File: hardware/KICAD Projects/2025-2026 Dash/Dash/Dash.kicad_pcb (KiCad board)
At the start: 2 copper layers, 200 x 75 mm, 41 parts, among them J1 TACH-SERVO, J2 SPEED-SERVO, J3 5V INPUT, J4 UPPER Button, J5 TO CAN CONNECTOR, J6 LOWER Button, U1 XIAO-ESP32-S3-SMD, U3 EA DOGM128W-6, Y1 ABM10AIG-16.000MHZ-4Z-T3

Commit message: Dash R1 Milestone
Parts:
- removed J3: 5V INPUT, Connector_Wire:SolderWire-0.75sqmm_1x02_P4.8mm_D1.25mm_OD2.3mm
- removed J5: TO CAN CONNECTOR, Connector_Wire:SolderWire-0.75sqmm_1x04_P4.8mm_D1.25mm_OD2.3mm
- removed the LOWER_AlphaDriver at (228.0, 108.4)
- removed the UPPER_AlphaDriver at (228.0, 83.9)
- added J7: DTF13-6P, DTF13-6P:TE_DTF13-6P, B.Cu at (232.8, 115.5)
- added LOWER_AlphaDriver: Alphanumeric Driver LOWER, Adafruit HT16K33 Breakout (Laptop):DIP1778W100P254L3556H630Q28N, B.Cu at (185.6, 105.6)
- added UPPER_AlphaDriver: Alphanumeric Driver UPPER, Adafruit HT16K33 Breakout (Laptop):DIP1778W100P254L3556H630Q28N, B.Cu at (185.8, 75.5)
- IC1: renamed from CAN CAN
- LOWER_D1-2, LOWER_D3-4, UPPER_D1-2, UPPER_D3-4: footprint Adafruit Dual Alphanumeric LED:1908 -> Adafruit Dual Alphanumeric LED (Laptop):1908
- moved G*** 164.8 mm to (230.6, 83.5)
- moved R1 53.9 mm to (138.6, 67.0)
- moved R2 49.4 mm to (138.6, 69.0)
- moved U3 48.0 mm to (152.0, 73.5), turned to -90 degrees
- moved C1 47.1 mm to (103.8, 120.4), turned to 90 degrees
- moved R3 44.9 mm to (138.6, 71.0)
- moved C2 44.6 mm to (106.2, 120.4), turned to 90 degrees
- moved C3 42.4 mm to (108.8, 120.4), turned to 90 degrees
- moved C4 40.4 mm to (111.4, 120.4), turned to 90 degrees
- moved J4 38.5 mm to (86.7, 60.0)
- moved C5 36.6 mm to (114.8, 119.5), turned to 180 degrees
- moved C6 33.9 mm to (120.0, 119.5), turned to 0 degrees
- moved C7 32.3 mm to (124.8, 119.5), turned to 0 degrees
- moved C8 32.2 mm to (129.2, 120.4), turned to 90 degrees
- moved C9 31.6 mm to (132.8, 119.5), turned to 0 degrees
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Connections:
- IC1 pad 26: GND -> CAN_GND
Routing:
- net GND: track 684.4 -> 568.1 mm, vias 7 -> 5
- net ROW14_UPPER: track 156.0 -> 44.5 mm, vias 3 -> 0
- net CAN_HIGH: track 69.2 -> 161.7 mm, vias 0 -> 2
- net ROW0_UPPER: track 141.0 -> 52.7 mm, vias 0 -> 1
- net CAN_LOW: track 63.9 -> 150.7 mm, vias 0 -> 2
- net COM_Digit1_LOWER: track 121.3 -> 38.4 mm
- net ROW1_UPPER: track 132.8 -> 54.4 mm, vias 1 -> 0
- net COM_Digit3_LOWER: track 82.2 -> 8.96 mm
- net COM_Digit2_LOWER: track 88.5 -> 24.3 mm
- net COM_Digit3_UPPER: track 67.1 -> 8.96 mm, vias 1 -> 0
- net COM_Digit2_UPPER: track 82.0 -> 24.3 mm
- net COM_Digit1_UPPER: track 94.9 -> 38.4 mm
- net ROW4_UPPER: track 162.3 -> 106.8 mm, vias 0 -> 1
- net COM_Digit4_LOWER: track 73.3 -> 18.7 mm
- net ROW6_LOWER: track 91.3 -> 37.3 mm
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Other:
- board text added: "C1-9: 1uF"
- board text added: "DASHBOARD REV. 1 Designed by Adam Esch in Tucson, Arizona January 25th, 2026"
- board text removed: "C1-4: 1uF"
- board text removed: "C5-9: 1uF"
- board text removed: "Designed by Adam Esch in Tucson, Arizona, on November 10th, 2025 DASHBOARD REV. 0"
- board text removed: "if this text is visible, congrats you've lost the game"

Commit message: Repo ready for ordering
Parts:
- moved G*** 47.5 mm to (81.5, 91.0)
- moved REF** 16.3 mm to (229.0, 128.0)
- moved REF** 16.0 mm to (229.0, 68.0)
- moved J7 9.44 mm to (227.0, 108.0), turned to -90 degrees
- moved G*** 6.35 mm to (225.0, 86.5)
- moved REF** 4.98 mm to (149.0, 63.0)
- moved REF** 4.27 mm to (95.0, 124.0)
- moved C1 3.00 mm to (103.8, 123.4)
- moved C11 3.00 mm to (135.7, 90.5)
- moved C12 3.00 mm to (132.0, 103.0)
- moved C13 3.00 mm to (121.0, 87.9)
- moved C14 3.00 mm to (129.5, 87.9)
- moved C2 3.00 mm to (106.2, 123.4)
- moved C3 3.00 mm to (108.8, 123.4)
- moved C4 3.00 mm to (111.4, 123.4)
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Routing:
- net GND: track 568.1 -> 592.0 mm, vias 5 -> 4
- net +5V: track 378.0 -> 358.4 mm
- net CAN_HIGH: track 161.7 -> 149.7 mm
- net CAN_LOW: track 150.7 -> 142.7 mm
- net ROW2_UPPER: track 84.6 -> 83.9 mm
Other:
- board size 200 x 75 mm -> 184 x 75 mm
- board text removed: "H L H L"
- board text removed: "L H L H"

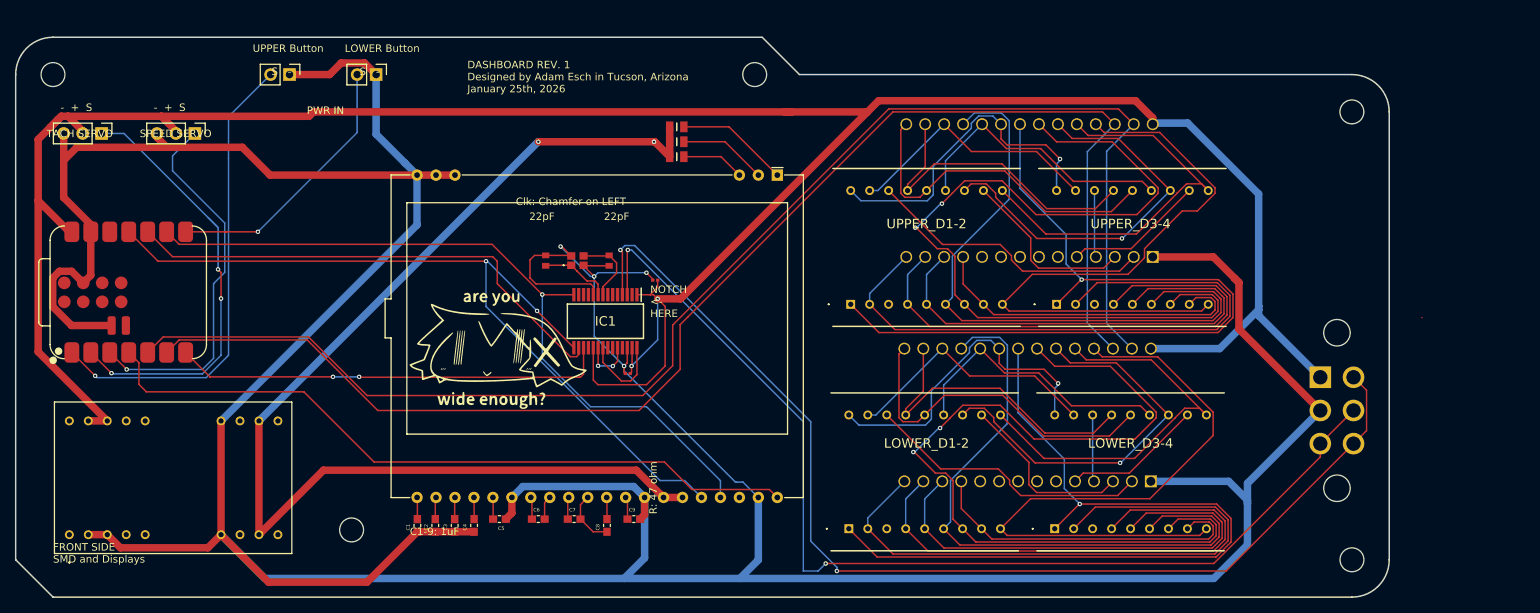
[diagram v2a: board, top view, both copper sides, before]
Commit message: Voltage Converter Modification
Old 5V-3.3V NON-isolated converter was out of stock everywhere, replaced it with ISOLATED unit with GNDs connected together lol
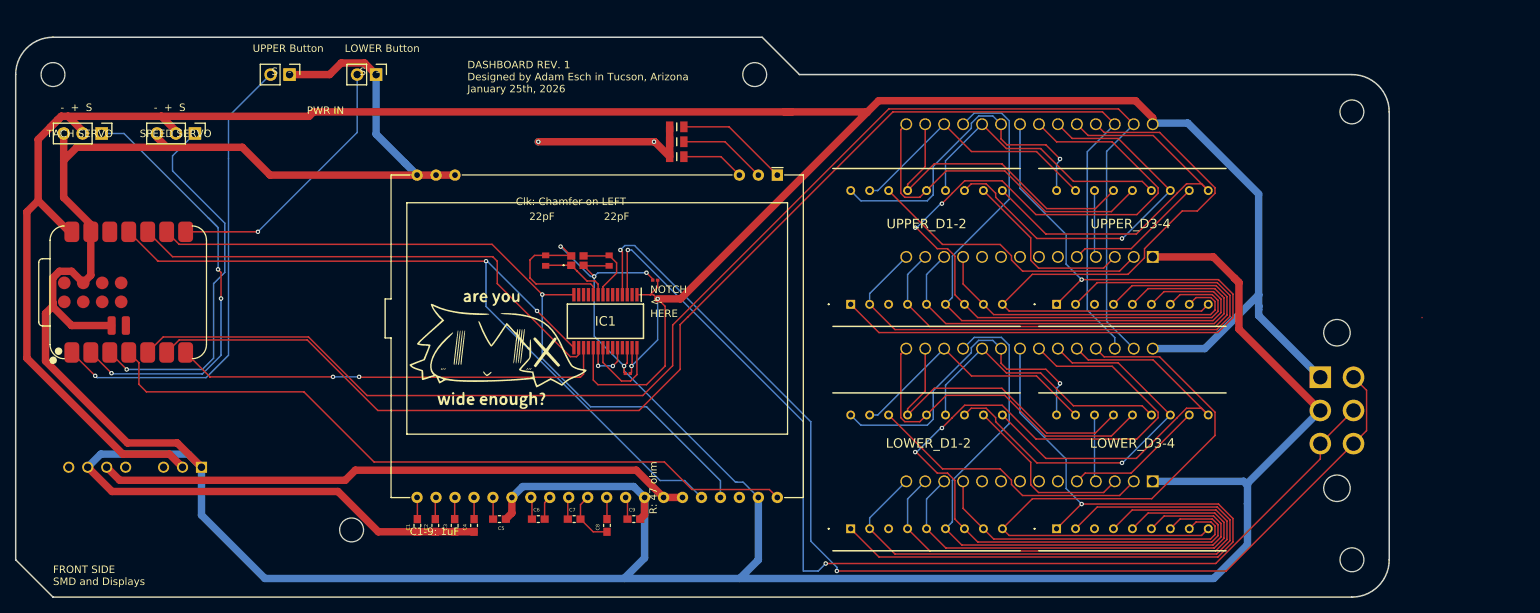
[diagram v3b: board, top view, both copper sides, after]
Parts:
- removed PS1: EC5A-05S33, EC5A-05S33:EC5A05S33
- added PS2: RS3K-053.3S_H3, RS3K-053.3S_H3:RS3K0533SH3, B.Cu at (74.9, 115.6)
- moved LOWER_AlphaDriver 0.25 mm to (185.8, 108.6)
- moved LOWER_D1-2 0.25 mm to (161.9, 123.8)
- moved LOWER_D3-4 0.25 mm to (189.4, 123.8)
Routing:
- net +3.3V: track 152.4 -> 102.4 mm
- net +5V: track 358.4 -> 371.7 mm
- net GND: track 592.0 -> 590.1 mm
